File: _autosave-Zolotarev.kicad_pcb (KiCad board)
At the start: 2 copper layers, 185 x 185 mm, 172 parts, among them J1 RF_IN, J2 RF_OUT, J3 Conn_02x05_Odd_Even, K1 G5LE-1, K10 G5LE-1, K11 G5LE-1, K12 G5LE-1, K13 G5LE-1, K14 G5LE-1, K2 G5LE-1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

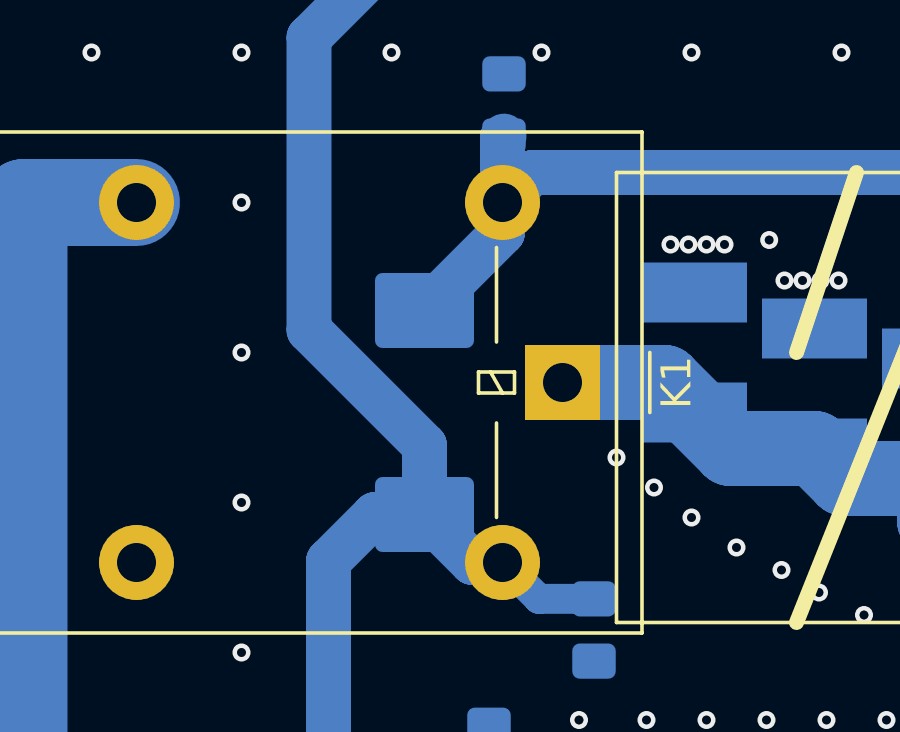
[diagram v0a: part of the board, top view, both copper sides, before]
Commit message: all bands routed, command connector to do
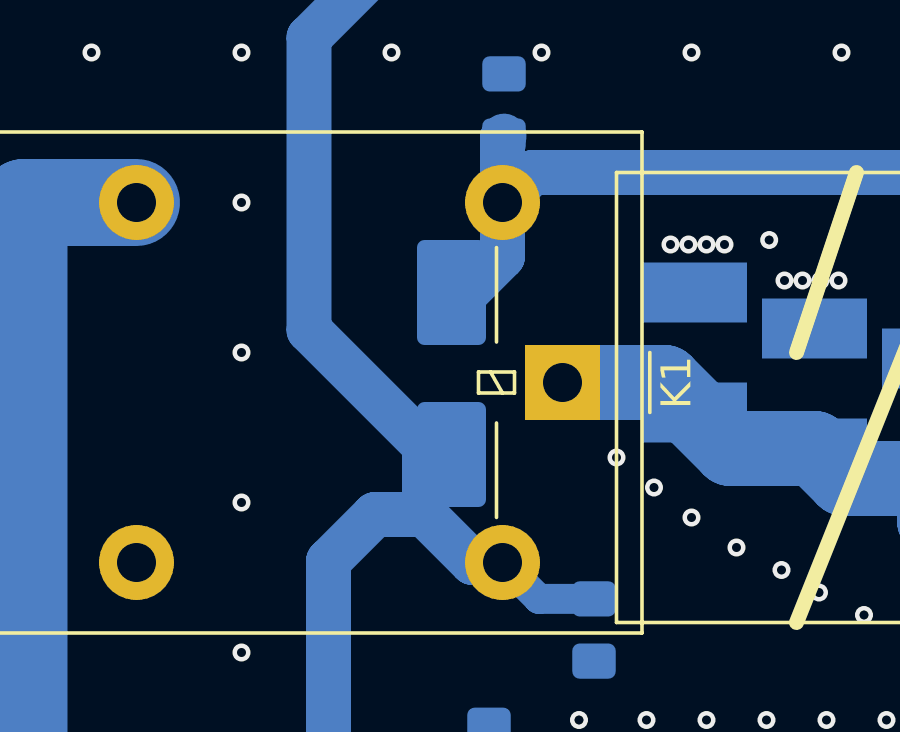
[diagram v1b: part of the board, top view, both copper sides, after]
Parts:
- D1: footprint Diode_SMD:D_SMC -> Diode_SMD:D_SMB_Handsoldering
- moved D1 1.58 mm to (75.5, 40.7)
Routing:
- net 160m: track 145.8 -> 144.6 mm
